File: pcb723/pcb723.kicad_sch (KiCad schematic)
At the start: 61 parts, among them J1 Conn_01x02_Pin, J2 Conn_01x02_Pin, J3 Conn_02x07_Odd_Even, J4 Conn_02x02_Odd_Even, J5 USB_C_Receptacle_USB2.0_16P, J6 Conn_02x13_Odd_Even, J7 Conn_02x14_Odd_Even, J8 Conn_02x13_Odd_Even, J9 Conn_02x12_Odd_Even, SW1 SW_Push, U1 STM32H723ZGT6, U2 AMS1117-3.3, Y1 8MHz 20pF

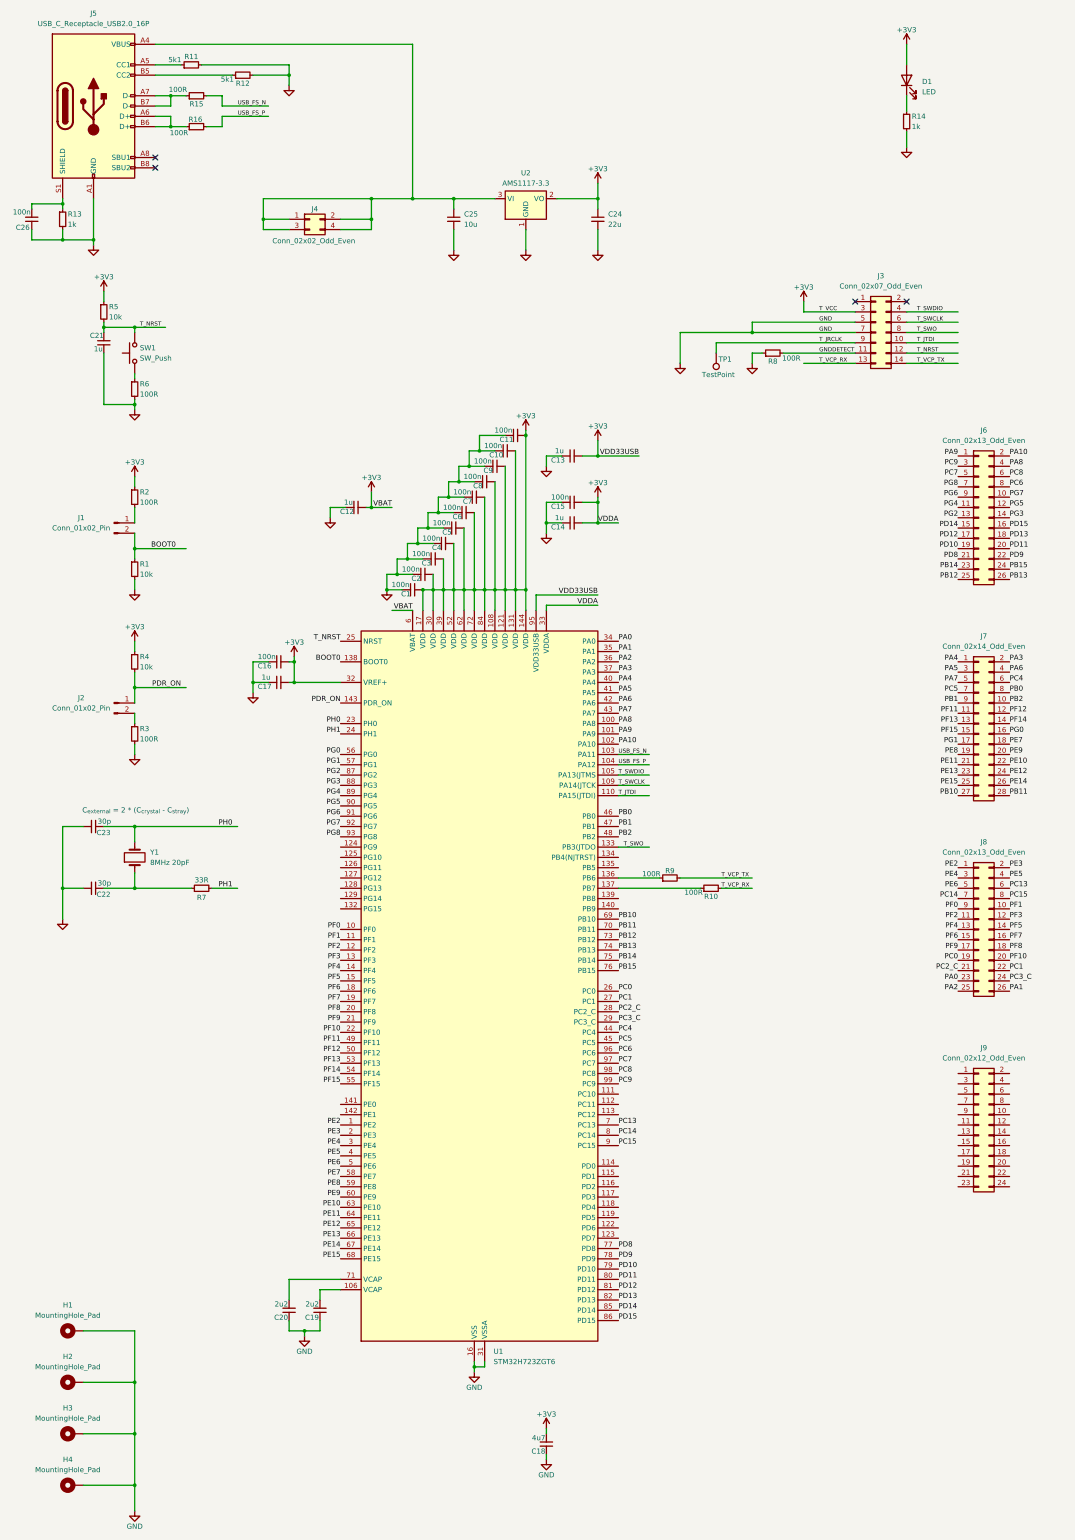
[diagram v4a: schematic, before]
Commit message: Add 4 LEDs
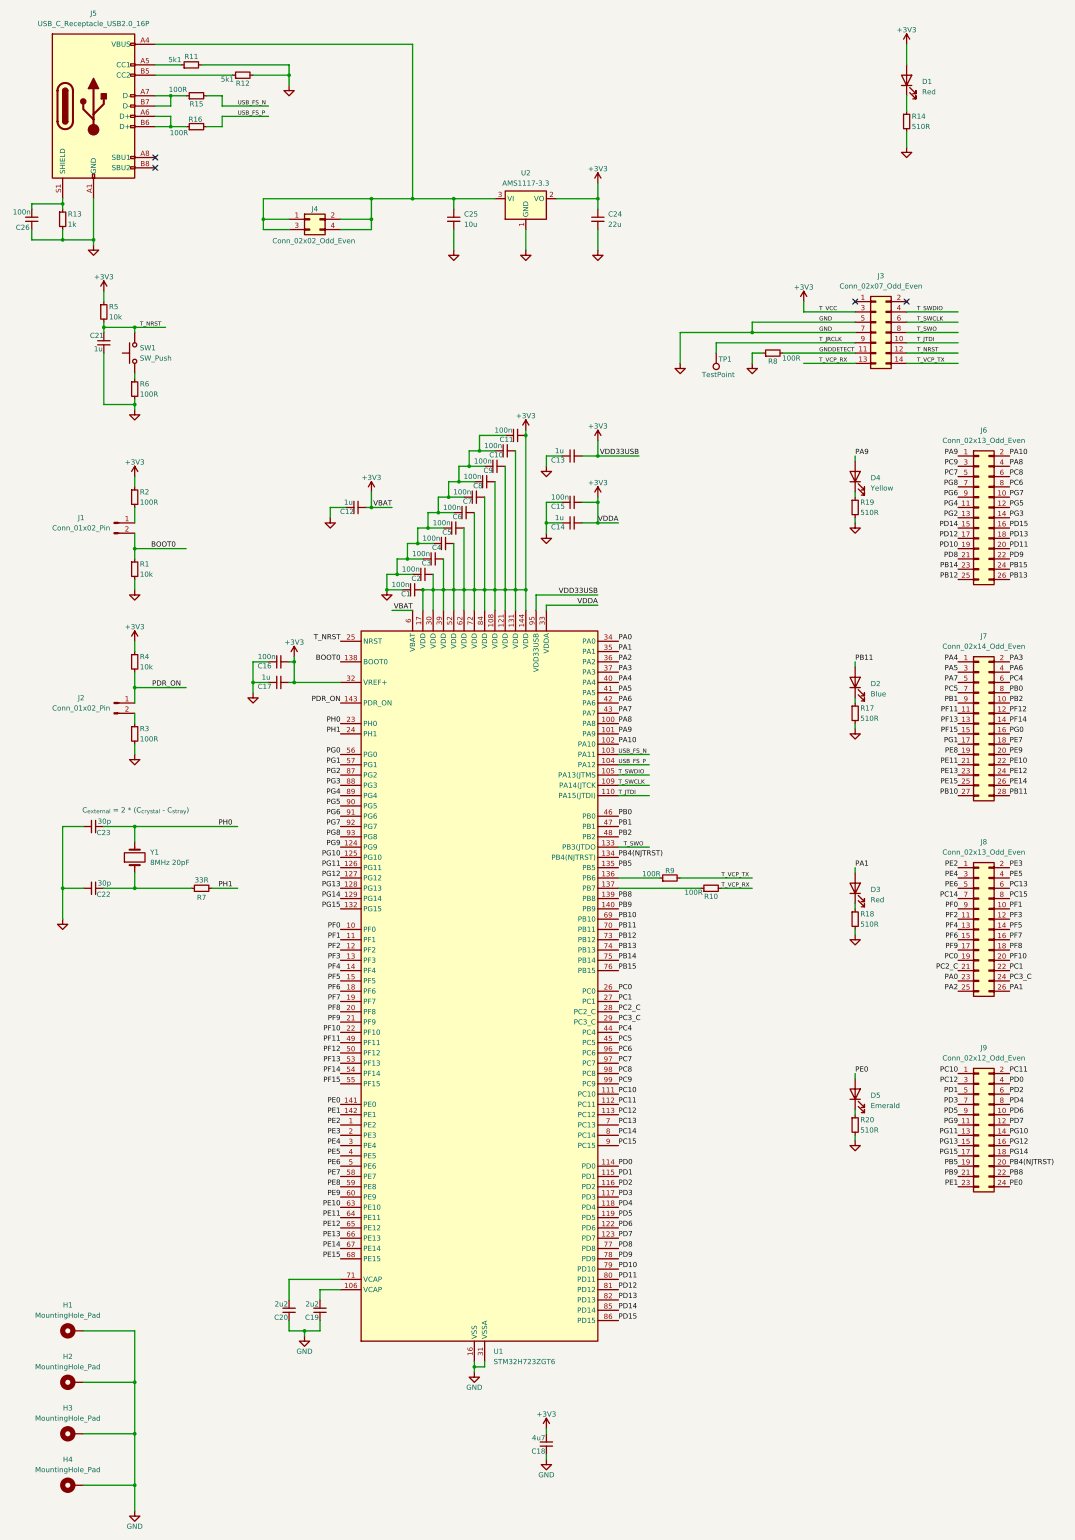
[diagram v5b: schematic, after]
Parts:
- added D2: Blue, LED_SMD:LED_0805_2012Metric, symbol Device:LED
- added D3: Red, LED_SMD:LED_0805_2012Metric, symbol Device:LED
- added D4: Yellow, LED_SMD:LED_0805_2012Metric, symbol Device:LED
- added D5: Emerald, LED_SMD:LED_0805_2012Metric, symbol Device:LED
- added R17, R18, R19, R20: 510R, Resistor_SMD:R_0402_1005Metric, symbol Device:R_Small
- D1: value LED -> Red
- R14: value 1k -> 510R; JLC# C11702 -> C25123
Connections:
- net GND: now also R17.2, R18.2, R19.2, R20.2
- net PA1: now also D3.2 (A)
- net PA9: now also D4.2 (A)
- net PB11: now also D2.2 (A)
- net PC10: now reaches U1.111 (PC10)
- net PC10: now also J9.1 (Pin_1)
- net PC11: now reaches U1.112 (PC11)
- net PC11: now also J9.2 (Pin_2)
- net PC12: now reaches U1.113 (PC12)
- net PC12: now also J9.3 (Pin_3)
- net PD0: now reaches U1.114 (PD0)
- net PD0: now also J9.4 (Pin_4)
- net PD1: now reaches U1.115 (PD1)
- net PD1: now also J9.5 (Pin_5)
- net PD2: now reaches U1.116 (PD2)
- net PD2: now also J9.6 (Pin_6)
- net PD3: now reaches U1.117 (PD3)
- net PD3: now also J9.7 (Pin_7)
- net PD4: now reaches U1.118 (PD4)
- net PD4: now also J9.8 (Pin_8)
- net PD5: now reaches U1.119 (PD5)
- net PD5: now also J9.9 (Pin_9)
- net PD6: now reaches U1.122 (PD6)
- net PD6: now also J9.10 (Pin_10)
- net PD7: now reaches U1.123 (PD7)
- net PD7: now also J9.12 (Pin_12)
- net PG9: now reaches U1.124 (PG9)
- net PG9: now also J9.11 (Pin_11)
- net PG10: now reaches U1.125 (PG10)
- net PG10: now also J9.14 (Pin_14)
- net PG11: now reaches U1.126 (PG11)
- net PG11: now also J9.13 (Pin_13)
- net PG12: now reaches U1.127 (PG12)
- net PG12: now also J9.16 (Pin_16)
- net PG13: now reaches U1.128 (PG13)
- net PG13: now also J9.15 (Pin_15)
- net PG14: now reaches U1.129 (PG14)
- net PG14: now also J9.18 (Pin_18)
- net PG15: now reaches U1.132 (PG15)
- net PG15: now also J9.17 (Pin_17)
- net PB4(NJTRST): now reaches U1.134 (PB4(NJTRST))
- net PB4(NJTRST): now also J9.20 (Pin_20)
- net PB5: now reaches U1.135 (PB5)
- net PB5: now also J9.19 (Pin_19)
- net PB8: now reaches U1.139 (PB8)
- net PB8: now also J9.22 (Pin_22)
- net PB9: now reaches U1.140 (PB9)
- net PB9: now also J9.21 (Pin_21)
- net PE0: now reaches U1.141 (PE0)
- net PE0: now also J9.24 (Pin_24), D5.2 (A)
- net PE1: now reaches U1.142 (PE1)
- net PE1: now also J9.23 (Pin_23)
- new net: D5.1 (K), R20.1
- new net: D3.1 (K), R18.1
- new net: D2.1 (K), R17.1
- new net: D4.1 (K), R19.1

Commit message: Complete schematic
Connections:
- net +5V: now reaches C25.1, J4.1 (Pin_1), J4.2 (Pin_2), J4.3 (Pin_3), J4.4 (Pin_4), J5.A4 (VBUS), J5.A9 (VBUS), J5.B4 (VBUS), J5.B9 (VBUS), U2.3 (VI)
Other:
- note added: "T_VCC"
- moved on the sheet: C1, C10, C11, C12, C13, C14, C15, C2, C3, C4, C5, C6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

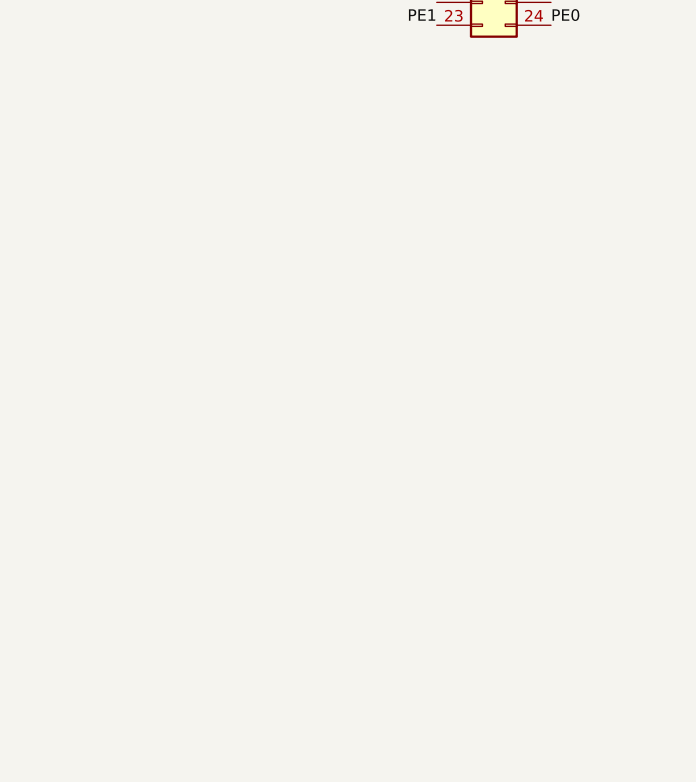
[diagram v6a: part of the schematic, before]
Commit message: Add power socket headers
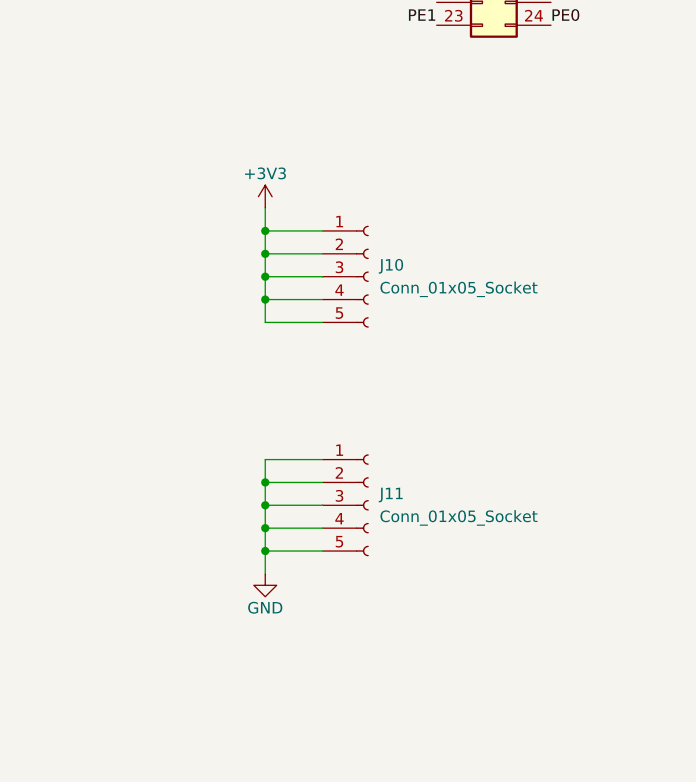
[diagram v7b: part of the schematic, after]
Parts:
- added J10, J11: Conn_01x05_Socket, Connector_PinSocket_2.54mm:PinSocket_1x05_P2.54mm_Vertical, symbol Connector:Conn_01x05_Socket
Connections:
- net +3V3: now also J10.1 (Pin_1), J10.2 (Pin_2), J10.3 (Pin_3), J10.4 (Pin_4), J10.5 (Pin_5)
- net GND: now also J11.1 (Pin_1), J11.2 (Pin_2), J11.3 (Pin_3), J11.4 (Pin_4), J11.5 (Pin_5)
